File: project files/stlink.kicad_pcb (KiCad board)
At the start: 2 copper layers, 38.1 x 17.8 mm, 62 parts, among them J1 USB_C_Receptacle_USB2.0, J2 SWD, J3 SELF, J4 TARGET, Q1 MMBT9013, U1 STM32F103CBTx, U2 AMS1117-3.3, Y1 8MHz

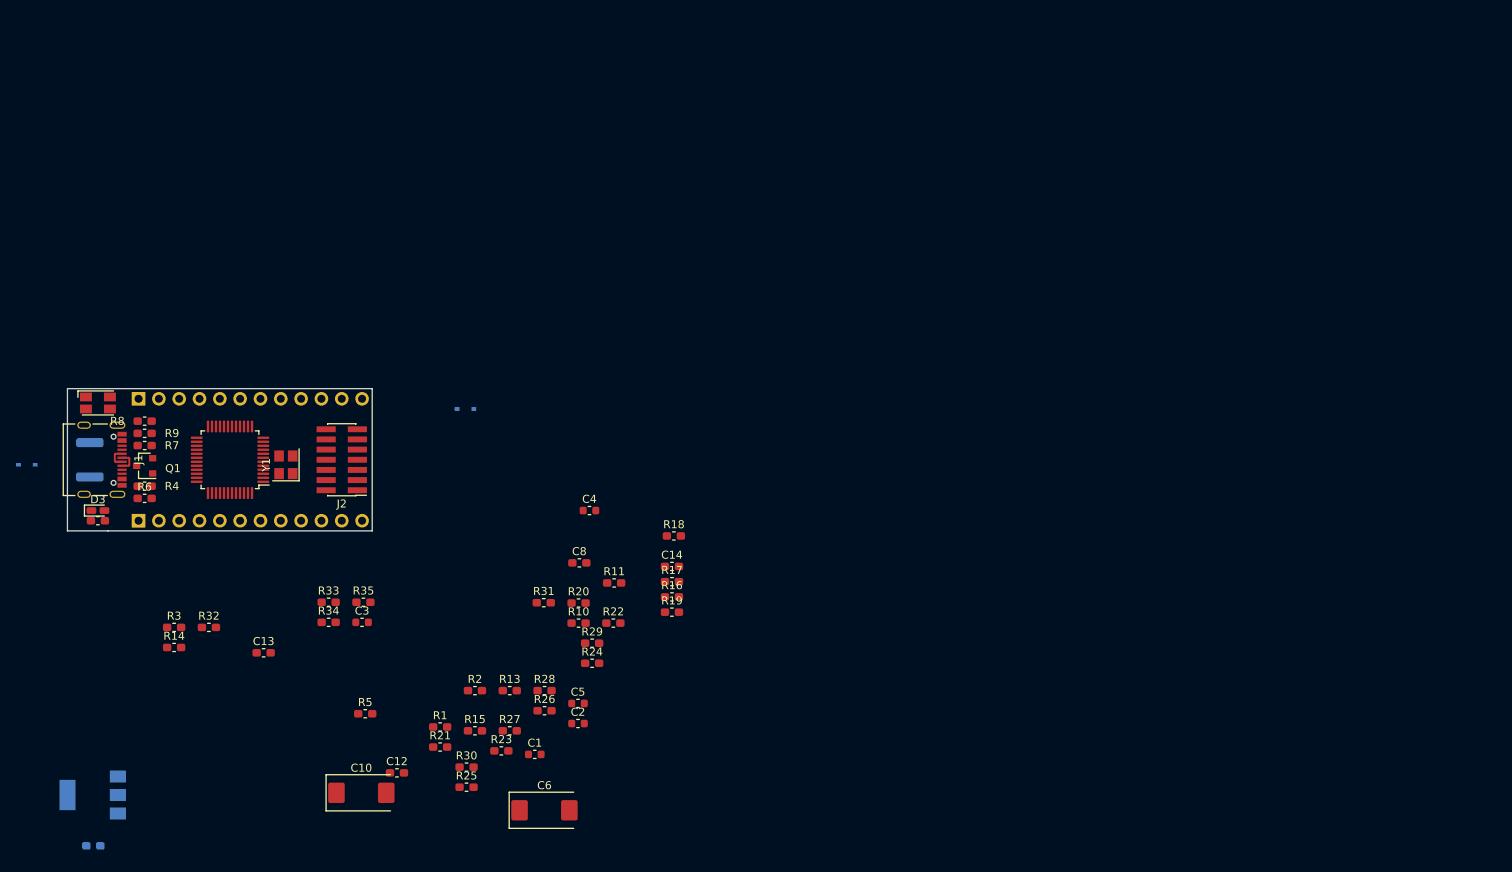
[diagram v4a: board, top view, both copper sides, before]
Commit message: Added possibility to power target from programmer
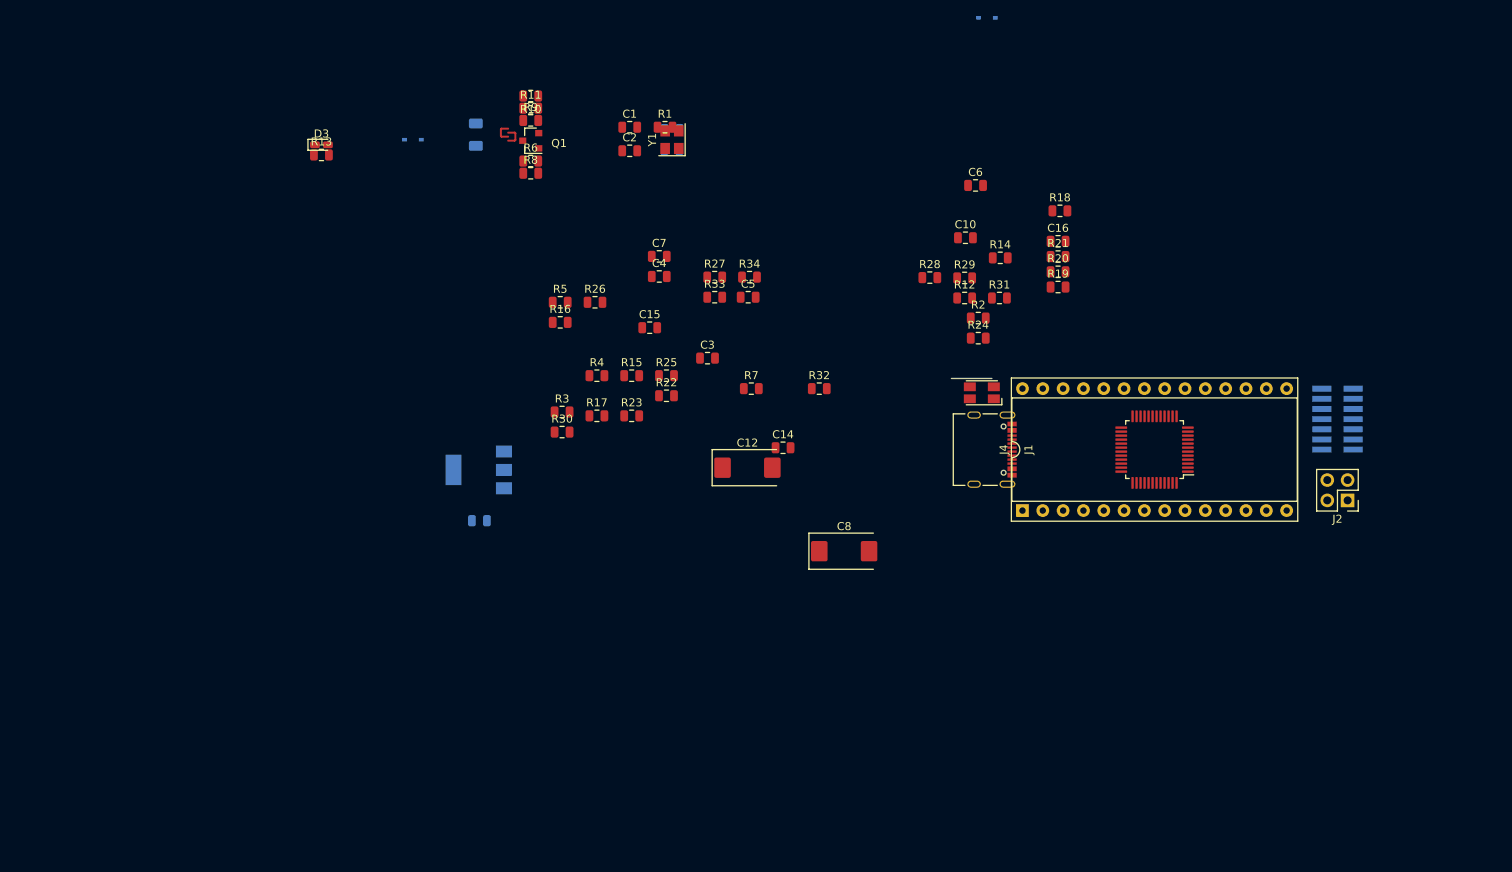
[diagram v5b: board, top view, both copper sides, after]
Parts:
- removed the J3 at (105.4, 125.7)
- removed the R23 at (150.8, 154.5)
- removed the R25 at (146.4, 159.0)
- removed the R30 at (146.4, 156.5)
- added C1: 100nF, Capacitor_SMD:C_0805_2012Metric, F.Cu at (166.8, 76.5)
- added C2: 1nF, Capacitor_SMD:C_0805_2012Metric, F.Cu at (166.8, 79.5)
- added J2: Power Target, Connector_PinHeader_2.54mm:PinHeader_2x02_P2.54mm_Vertical, F.Cu at (256.5, 123.2)
- added R1: 1M, Resistor_SMD:R_0805_2012Metric, F.Cu at (171.2, 76.5)
- added R32: 22R, Resistor_SMD:R_0805_2012Metric, F.Cu at (190.5, 109.2)
- C10: renamed from C8; footprint Capacitor_SMD:C_0603_1608Metric_Pad1.05x0.95mm_HandSolder -> Capacitor_SMD:C_0805_2012Metric
- C11: renamed from C9; footprint Capacitor_SMD:C_0603_1608Metric_Pad1.05x0.95mm_HandSolder -> Capacitor_SMD:C_0805_2012Metric
- C13: renamed from C11; footprint Capacitor_SMD:C_0603_1608Metric_Pad1.05x0.95mm_HandSolder -> Capacitor_SMD:C_0805_2012Metric
- C14: renamed from C12; footprint Capacitor_SMD:C_0603_1608Metric_Pad1.05x0.95mm_HandSolder -> Capacitor_SMD:C_0805_2012Metric
- C15: renamed from C13; footprint Capacitor_SMD:C_0603_1608Metric_Pad1.05x0.95mm_HandSolder -> Capacitor_SMD:C_0805_2012Metric
- C16: renamed from C14; footprint Capacitor_SMD:C_0603_1608Metric_Pad1.05x0.95mm_HandSolder -> Capacitor_SMD:C_0805_2012Metric
- C3: renamed from C1; footprint Capacitor_SMD:C_0603_1608Metric -> Capacitor_SMD:C_0805_2012Metric
- C4: renamed from C2; footprint Capacitor_SMD:C_0603_1608Metric -> Capacitor_SMD:C_0805_2012Metric
- C5: renamed from C3; footprint Capacitor_SMD:C_0603_1608Metric -> Capacitor_SMD:C_0805_2012Metric
- C6: renamed from C4; footprint Capacitor_SMD:C_0603_1608Metric -> Capacitor_SMD:C_0805_2012Metric
- C7: renamed from C5; footprint Capacitor_SMD:C_0603_1608Metric -> Capacitor_SMD:C_0805_2012Metric
- C9: renamed from C7; footprint Capacitor_SMD:C_0603_1608Metric_Pad1.05x0.95mm_HandSolder -> Capacitor_SMD:C_0805_2012Metric
- F1: footprint Fuse:Fuse_1812_4532Metric -> Resistor_SMD:R_1206_3216Metric
- J3: renamed from J2; moved to B.Cu
- J4: value TARGET -> Side Connectors; footprint Connector_PinHeader_2.54mm:PinHeader_1x12_P2.54mm_Vertical -> Package_DIP:DIP-28_W15.24mm_Socket; moved to F.Cu
- R10: renamed from R8; footprint Resistor_SMD:R_0603_1608Metric_Pad1.05x0.95mm_HandSolder -> Resistor_SMD:R_0805_2012Metric
- R11: renamed from R9; footprint Resistor_SMD:R_0603_1608Metric_Pad1.05x0.95mm_HandSolder -> Resistor_SMD:R_0805_2012Metric
- R12: renamed from R10; footprint Resistor_SMD:R_0603_1608Metric_Pad1.05x0.95mm_HandSolder -> Resistor_SMD:R_0805_2012Metric
- R13: renamed from R12; footprint Resistor_SMD:R_0603_1608Metric_Pad1.05x0.95mm_HandSolder -> Resistor_SMD:R_0805_2012Metric
- R14: renamed from R11; footprint Resistor_SMD:R_0603_1608Metric_Pad1.05x0.95mm_HandSolder -> Resistor_SMD:R_0805_2012Metric
- R15: renamed from R13; footprint Resistor_SMD:R_0603_1608Metric_Pad1.05x0.95mm_HandSolder -> Resistor_SMD:R_0805_2012Metric
- R16: renamed from R14; footprint Resistor_SMD:R_0603_1608Metric_Pad1.05x0.95mm_HandSolder -> Resistor_SMD:R_0805_2012Metric
- R17: renamed from R15; footprint Resistor_SMD:R_0603_1608Metric_Pad1.05x0.95mm_HandSolder -> Resistor_SMD:R_0805_2012Metric
- R18, R19, R24: footprint Resistor_SMD:R_0603_1608Metric_Pad1.05x0.95mm_HandSolder -> Resistor_SMD:R_0805_2012Metric
- R2: renamed from R29; footprint Resistor_SMD:R_0603_1608Metric_Pad1.05x0.95mm_HandSolder -> Resistor_SMD:R_0805_2012Metric
- R20: renamed from R16; footprint Resistor_SMD:R_0603_1608Metric_Pad1.05x0.95mm_HandSolder -> Resistor_SMD:R_0805_2012Metric
- R21: renamed from R17; footprint Resistor_SMD:R_0603_1608Metric_Pad1.05x0.95mm_HandSolder -> Resistor_SMD:R_0805_2012Metric
- R22: renamed from R26; footprint Resistor_SMD:R_0603_1608Metric_Pad1.05x0.95mm_HandSolder -> Resistor_SMD:R_0805_2012Metric
- R23: renamed from R27; footprint Resistor_SMD:R_0603_1608Metric_Pad1.05x0.95mm_HandSolder -> Resistor_SMD:R_0805_2012Metric
- R25: renamed from R28; footprint Resistor_SMD:R_0603_1608Metric_Pad1.05x0.95mm_HandSolder -> Resistor_SMD:R_0805_2012Metric
- R26: renamed from R32; footprint Resistor_SMD:R_0603_1608Metric_Pad1.05x0.95mm_HandSolder -> Resistor_SMD:R_0805_2012Metric
- R27: renamed from R33; footprint Resistor_SMD:R_0603_1608Metric_Pad1.05x0.95mm_HandSolder -> Resistor_SMD:R_0805_2012Metric
- R28: renamed from R31; footprint Resistor_SMD:R_0603_1608Metric_Pad1.05x0.95mm_HandSolder -> Resistor_SMD:R_0805_2012Metric
- R29: renamed from R20; footprint Resistor_SMD:R_0603_1608Metric_Pad1.05x0.95mm_HandSolder -> Resistor_SMD:R_0805_2012Metric
- R3: renamed from R1; footprint Resistor_SMD:R_0603_1608Metric_Pad1.05x0.95mm_HandSolder -> Resistor_SMD:R_0805_2012Metric
- R30: renamed from R21; footprint Resistor_SMD:R_0603_1608Metric_Pad1.05x0.95mm_HandSolder -> Resistor_SMD:R_0805_2012Metric
- R31: renamed from R22; footprint Resistor_SMD:R_0603_1608Metric_Pad1.05x0.95mm_HandSolder -> Resistor_SMD:R_0805_2012Metric
- R33: renamed from R34; footprint Resistor_SMD:R_0603_1608Metric_Pad1.05x0.95mm_HandSolder -> Resistor_SMD:R_0805_2012Metric
- R34: renamed from R35; footprint Resistor_SMD:R_0603_1608Metric_Pad1.05x0.95mm_HandSolder -> Resistor_SMD:R_0805_2012Metric
- R4: renamed from R2; footprint Resistor_SMD:R_0603_1608Metric_Pad1.05x0.95mm_HandSolder -> Resistor_SMD:R_0805_2012Metric
- R5: renamed from R3; footprint Resistor_SMD:R_0603_1608Metric_Pad1.05x0.95mm_HandSolder -> Resistor_SMD:R_0805_2012Metric
- R6: renamed from R4; footprint Resistor_SMD:R_0603_1608Metric_Pad1.05x0.95mm_HandSolder -> Resistor_SMD:R_0805_2012Metric
- R7: renamed from R5; footprint Resistor_SMD:R_0603_1608Metric_Pad1.05x0.95mm_HandSolder -> Resistor_SMD:R_0805_2012Metric
- R8: renamed from R6; footprint Resistor_SMD:R_0603_1608Metric_Pad1.05x0.95mm_HandSolder -> Resistor_SMD:R_0805_2012Metric
- R9: renamed from R7; footprint Resistor_SMD:R_0603_1608Metric_Pad1.05x0.95mm_HandSolder -> Resistor_SMD:R_0805_2012Metric
- moved J3 124.6 mm to (255.3, 113.0), turned to 0 degrees
- moved U1 115.6 mm to (232.4, 116.8)
- moved J4 111.4 mm to (215.9, 124.5), turned to 90 degrees
- moved J1 111.3 mm to (212.1, 116.8)
- moved D2 110.5 mm to (210.8, 109.7), turned to 180 degrees
- moved D4 81.5 mm to (211.5, 62.9)
- moved C12 63.1 mm to (181.5, 119.1)
- moved C10 63.1 mm to (208.8, 90.4)
- moved C13 63.1 mm to (148.0, 125.7)
- moved C5 63.1 mm to (181.6, 97.8)
- moved F1 63.1 mm to (147.6, 77.5)
- moved R18 63.1 mm to (220.6, 87.0)
- moved R31 63.1 mm to (213.0, 97.9)
- moved R33 63.1 mm to (177.4, 97.8)
- moved C11 63.1 mm to (172.1, 76.8)
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- renumbered C10 to C12, C6 to C8
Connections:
- net /T_JTCK renamed /T_SWDCLK
- net /T_JTMS renamed /T_SWDIO
- C10 pad 2: GNDREF -> GND_detect(h)
- C11 pad 2: GNDREF -> GND_detect(h)
- C12 pad 2: GNDREF -> GND_detect(h)
- C13 pad 2: GNDREF -> GND_detect(h)
- C14 pad 1: BOOT_0h -> BOOT_0(h)
- C14 pad 2: GNDREF -> GND_detect(h)
- C15 pad 1: Self_NRSTh -> Self_NRST(h)
- C15 pad 2: GNDREF -> GND_detect(h)
- C16 pad 1: /AIN -> GND_detect(h)
- C16 pad 2: GNDREF -> /AIN
- C3 pad 2: GNDREF -> GND_detect(h)
- C4 pad 2: GNDREF -> GND_detect(h)
- C5 pad 2: GNDREF -> GND_detect(h)
- C6 pad 2: GNDREF -> GND_detect(h)
- C7 pad 2: GNDREF -> GND_detect(h)
- C8 pad 2: GNDREF -> GND_detect(h)
- C9 pad 2: GNDREF -> GND_detect(h)
- D2 pad 1: Net-(D2-Pad1) -> GND_detect(h)
- D2 pad 2: GNDREF -> Net-(D2-Pad2)
- D3 pad 1: GNDREF -> GND_detect(h)
- J1 pad A1: GNDREF -> GND_detect(h)
- J1 pad A12: GNDREF -> GND_detect(h)
- J1 pad A8: Net-(J1-PadA8) -> (no net)
- J1 pad B1: GNDREF -> GND_detect(h)
- J1 pad B12: GNDREF -> GND_detect(h)
- J1 pad B8: Net-(J1-PadB8) -> (no net)
- J1 pad S1: GNDREF -> Net-(C1-Pad1)
- J3 pad 1: Net-(J2-Pad1) -> (no net)
- J3 pad 12: T_NRST_SWDh -> T_NRST_SWD(h)
- J3 pad 13: T_VCP_RXh -> T_VCP_RX(h)
- J3 pad 14: T_VCP_TXh -> T_VCP_TX(h)
- J3 pad 2: Net-(J2-Pad2) -> (no net)
- J3 pad 4: T_JTMS-T_SWDIO(h) -> T_SWDIO(h)
- J3 pad 5: GNDREF -> GND_detect(h)
- J3 pad 6: T_JTLK(h) -> T_SWDCLK(h)
- J3 pad 7: GNDREF -> GND_detect(h)
- J3 pad 8: T_JTDO-T_SWO(h) -> T_SWO(h)
- J3 pad 9: T_JTLK(h) -> (no net)
- J4 pad 1: T_Vref -> +5V
- J4 pad 10: T_SWDIOh -> Self_SWDCLK(h)
- J4 pad 11: T_NRST_SWDh -> GND_detect(h)
- J4 pad 12: T_SWOh -> Self_SWDIO(h)
- J4 pad 2: T_SWIMh -> +3V3
- J4 pad 3: GNDREF -> BOOT_0(h)
- J4 pad 4: T_NRST_SWIMh -> +3V3
- J4 pad 5: T_VCP_RXh -> Self_TX(h)
- J4 pad 6: T_VCP_TXh -> Self_RX(h)
- J4 pad 7: T_Vref -> GND_detect(h)
- J4 pad 8: T_SWDCLKh -> (no net)
- J4 pad 9: GNDREF -> +3V3
- R12 pad 1: GNDREF -> GND_detect(h)
- R13 pad 1: Net-(D2-Pad1) -> /STLINK_LED
- R13 pad 2: /STLINK_LED -> Net-(D2-Pad2)
- R15 pad 1: BOOT_0h -> BOOT_0(h)
- R15 pad 2: GNDREF -> GND_detect(h)
- R17 pad 1: Self_NRSTh -> Self_NRST(h)
- R18 pad 2: GNDREF -> GND_detect(h)
- R2 pad 1: /PC13 -> GND_detect(h)
- R2 pad 2: GNDREF -> Net-(R2-Pad2)
- R21 pad 2: GNDREF -> GND_detect(h)
- R26 pad 2: T_SWIMh -> T_SWIM(h)
- R27 pad 2: T_NRST_SWIMh -> T_NRST_SWIM(h)
- R28 pad 1: T_JTMS-T_SWDIO(h) -> T_SWDIO(h)
- R29 pad 1: T_NRST_SWDh -> T_NRST_SWD(h)
- R3 pad 2: GNDREF -> GND_detect(h)
- R30 pad 1: T_JTLK(h) -> T_SWDCLK(h)
- R31 pad 1: T_JTDO-T_SWO(h) -> T_SWO(h)
- R33 pad 1: T_VCP_TXh -> T_VCP_TX(h)
- R34 pad 1: T_VCP_RXh -> T_VCP_RX(h)
- R4 pad 2: GNDREF -> GND_detect(h)
- R5 pad 2: Self_TXh -> Self_TX(h)
- R9 pad 2: Self_RXh -> Self_RX(h)
- U1 pad 11: Net-(U1-Pad11) -> (no net)
- U1 pad 14: Net-(U1-Pad14) -> (no net)
- U1 pad 16: /T_JTDO -> (no net)
- U1 pad 19: /T_JRST -> (no net)
- U1 pad 2: /PC13 -> Net-(R2-Pad2)
- U1 pad 20: GNDREF -> GND_detect(h)
- U1 pad 23: GNDREF -> GND_detect(h)
- U1 pad 28: Net-(U1-Pad28) -> (no net)
- U1 pad 29: Net-(U1-Pad29) -> (no net)
- U1 pad 3: /PC14 -> (no net)
- U1 pad 30: Self_TXh -> Self_TX(h)
- U1 pad 31: Self_RXh -> Self_RX(h)
- U1 pad 34: Self_SWDIOh -> Self_SWDIO(h)
- U1 pad 35: GNDREF -> GND_detect(h)
- U1 pad 37: Self_SWDCLKh -> Self_SWDCLK(h)
- U1 pad 39: Self_SWOh -> Self_SWO(h)
- U1 pad 4: Net-(U1-Pad4) -> (no net)
- U1 pad 40: Net-(U1-Pad40) -> (no net)
- U1 pad 44: BOOT_0h -> BOOT_0(h)
- U1 pad 47: GNDREF -> GND_detect(h)
- U1 pad 7: Self_NRSTh -> Self_NRST(h)
- U1 pad 8: GNDREF -> GND_detect(h)
- U2 pad 1: GNDREF -> GND_detect(h)
- Y1 pad 2: Net-(Y1-Pad2) -> GND_detect(h)
- Y1 pad 4: Net-(Y1-Pad4) -> GND_detect(h)
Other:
- board outline removed

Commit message: minor tracing
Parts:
- removed the J4 at (215.9, 124.5)
- added J3: Self, Connector_PinHeader_2.54mm:PinHeader_1x14_P2.54mm_Vertical, B.Cu at (215.9, 124.5)
- added J5: Target, Connector_PinHeader_2.54mm:PinHeader_1x14_P2.54mm_Vertical, B.Cu at (215.9, 109.2)
- added U2: STM32F103CBUx, Package_DFN_QFN:QFN-48-1EP_7x7mm_P0.5mm_EP5.6x5.6mm, F.Cu at (232.4, 116.8)
- J1: value USB_C_Receptacle_USB2.0 -> USB Type C
- J4: renamed from J3; value SWD -> STDC-14; moved to F.Cu
- moved C9 78.0 mm to (239.3, 116.5)
- moved Y1 77.9 mm to (239.3, 117.6)
- moved C8 77.9 mm to (239.3, 118.7)
- moved Q1 73.6 mm to (216.7, 117.6)
- moved R8 73.6 mm to (216.7, 115.1)
- moved R10 73.6 mm to (216.7, 113.5)
- moved R5 73.6 mm to (216.7, 120.1)
- moved R7 73.6 mm to (216.7, 121.7)
- moved R9 73.6 mm to (216.7, 112.0)
- moved J2 46.4 mm to (210.2, 121.9), turned to 0 degrees
- moved J4 9.63 mm to (246.4, 116.8), turned to 180 degrees
- moved R1 5.89 mm to (168.9, 71.1)
- moved J1 0.76 mm to (211.3, 116.8)
- moved D2 0.64 mm to (211.5, 109.7)
- renumbered C8 to C10, C14 to C11, C15 to C12, C10 to C13, C12 to C14, C13 to C15, C5 to C4, C4 to C5, C9 to C8, C11 to C9, D4 to D3, D3 to D4, R11 to R10, R12 to R11, R13 to R12, R14 to R13, R15 to R14, R2 to R15, R17 to R16, R18 to R17, R16 to R18, R3 to R2, R4 to R3, R5 to R4, R6 to R5, R7 to R6, R8 to R7, R9 to R8, R10 to R9, U2 to U3
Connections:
- net Net-(R2-Pad2) renamed /Board_ID
- C4 pad 1: +3V3 -> Net-(C4-Pad1)
- C6 pad 1: +3V3 -> Net-(C4-Pad1)
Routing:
- net /STLINK_OSC_IN: track 0.00 -> 4.56 mm
- net /D-: track 2.72 -> 0.00 mm
- net /D+: track 2.71 -> 0.00 mm
- net /STLINK_OST_OUT: track 0.00 -> 2.09 mm
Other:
- board outline added: 52.1 x 17.8 mm

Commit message: new references
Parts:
- C1, C16, C2: footprint Capacitor_SMD:C_0805_2012Metric -> Capacitor_SMD:C_0603_1608Metric; moved to B.Cu
- C11, C12, C13, C15, C3, C4, C5, C6, C7, C8, C9: footprint Capacitor_SMD:C_0805_2012Metric -> Capacitor_SMD:C_0603_1608Metric
- Q1: moved to B.Cu
- R1, R15, R17, R19, R20, R21, R8: footprint Resistor_SMD:R_0805_2012Metric -> Resistor_SMD:R_0603_1608Metric; moved to B.Cu
- R10, R11, R12, R13, R14, R16, R18, R2, R22, R23, R24, R25, R26, R27, R28, R29, R3, R30, R31, R32, R33, R34, R4, R5, R6, R7, R9: footprint Resistor_SMD:R_0805_2012Metric -> Resistor_SMD:R_0603_1608Metric
- moved J2 61.2 mm to (271.1, 127.0)
- moved R1 60.7 mm to (210.2, 115.6), turned to 180 degrees
- moved C1 59.6 mm to (210.2, 117.5)
- moved C2 58.9 mm to (210.2, 119.4)
- moved R15 34.1 mm to (238.1, 120.2), turned to 90 degrees
- moved D3 30.4 mm to (224.8, 90.2)
- moved R8 9.45 mm to (226.1, 116.1), turned to 270 degrees
- moved R5 3.94 mm to (216.7, 116.2)
- moved R7 3.56 mm to (216.7, 118.1)
- moved R17 1.92 mm to (220.3, 88.9), turned to 180 degrees
- turned R19 to 180 degrees
- turned R21 to 180 degrees
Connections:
- C4 pad 1: Net-(C4-Pad1) -> +3V3
- C6 pad 1: Net-(C4-Pad1) -> +3V3
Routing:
- net /STLINK_OSC_IN: track 4.56 -> 0.00 mm
- net /STLINK_OST_OUT: track 2.09 -> 0.00 mm
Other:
- board size 52.1 x 17.8 mm -> 43.2 x 17.8 mm

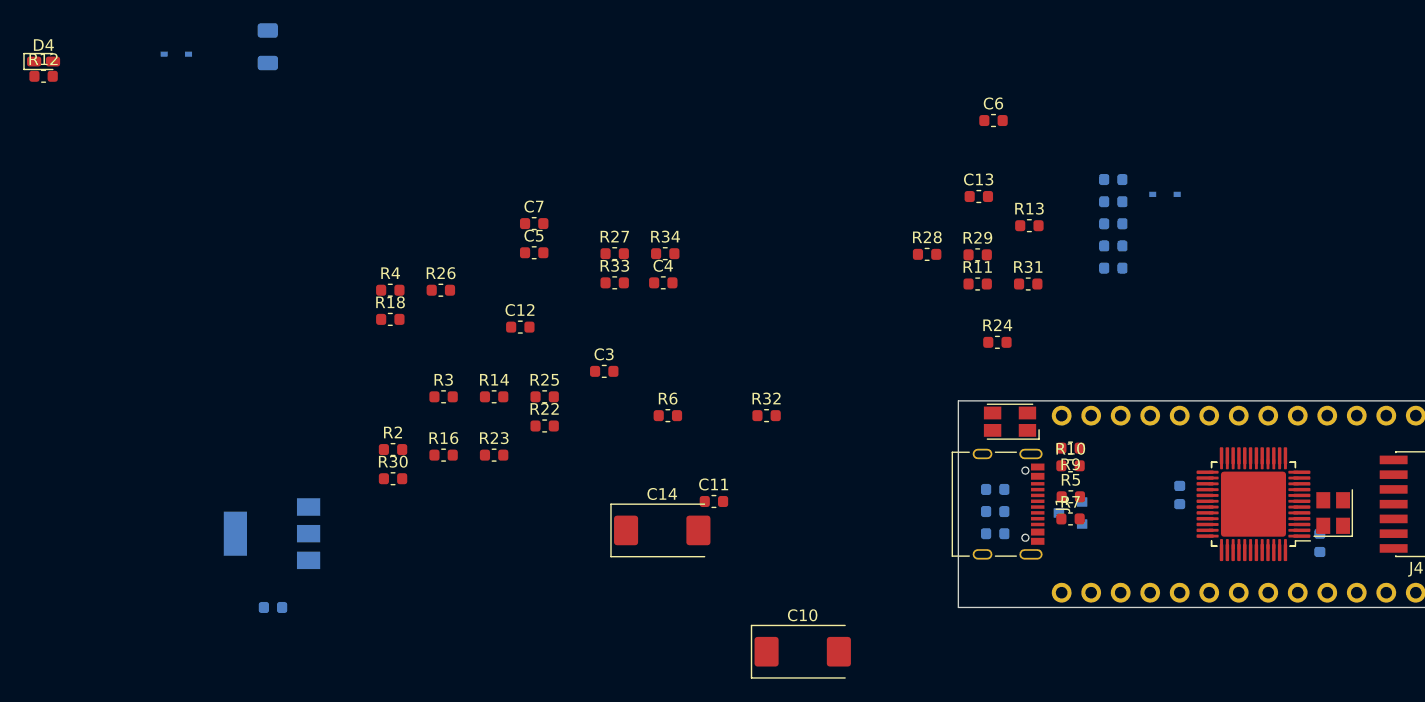
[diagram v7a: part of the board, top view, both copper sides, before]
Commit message: added reference for BMP
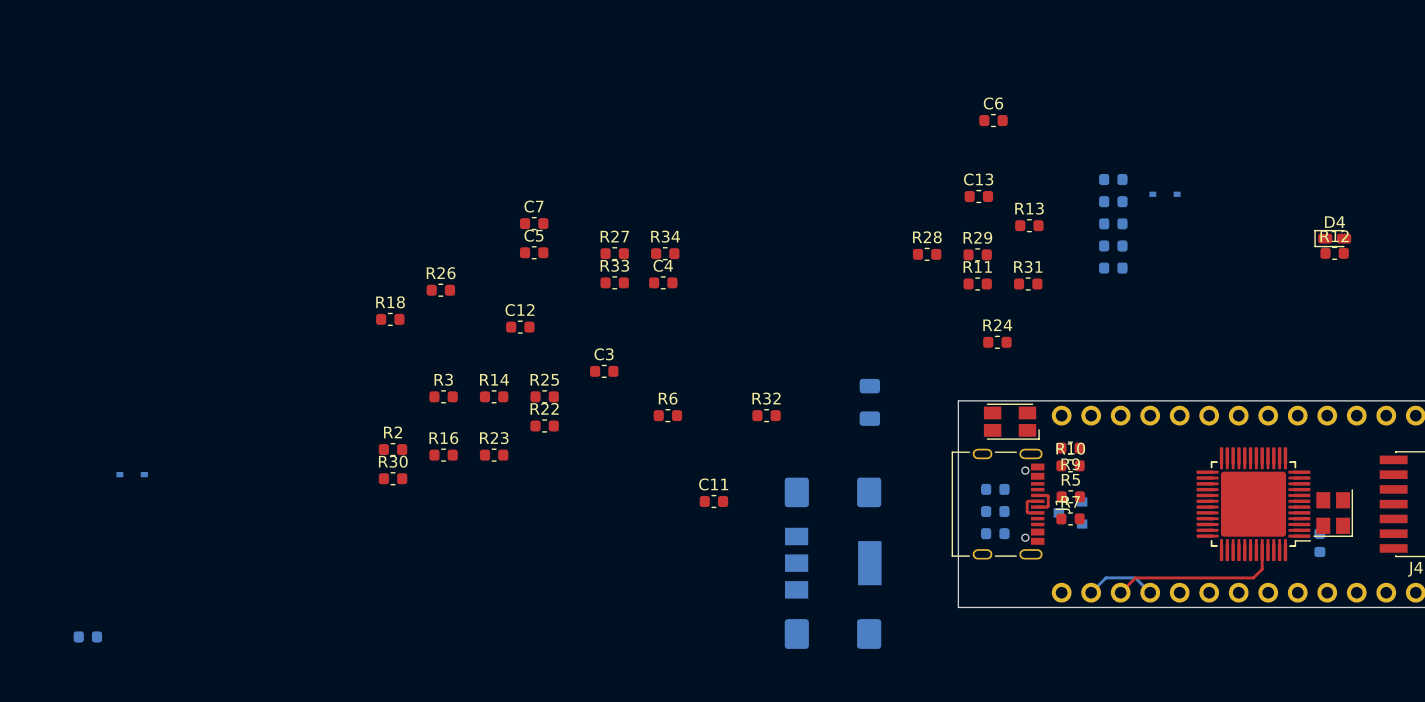
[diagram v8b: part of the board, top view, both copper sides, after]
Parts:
- removed R4, R8: 10R, Resistor_SMD:R_0603_1608Metric
- C10, C14: moved to B.Cu
- moved D4 112.2 mm to (239.4, 94.0)
- moved R12 112.2 mm to (239.4, 95.2)
- moved F1 60.2 mm to (199.4, 108.1)
- moved U3 48.4 mm to (196.2, 121.9), turned to 0 degrees
- moved D1 36.4 mm to (135.9, 114.3)
- moved C14 17.2 mm to (196.2, 128.0), turned to 180 degrees
- moved C15 16.1 mm to (132.1, 128.3)
- moved C10 14.0 mm to (196.2, 115.8), turned to 180 degrees
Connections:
- C11 pad 1: BOOT_0(h) -> GND_detect(h)
- C11 pad 2: GND_detect(h) -> BOOT_0(h)
- C12 pad 1: Self_NRST(h) -> GND_detect(h)
- C12 pad 2: GND_detect(h) -> Self_NRST(h)
- R12 pad 1: /STLINK_LED -> Net-(D2-Pad3)
- R12 pad 2: Net-(D2-Pad2) -> Self_TX(h)
- R13 pad 1: Net-(D2-Pad3) -> Net-(D2-Pad2)
- R13 pad 2: /STLINK_LED -> Self_TX(h)
- R31 pad 2: /T_SWO -> Self_RX(h)
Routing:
- net BOOT_0(h): track 0.00 -> 14.5 mm
- net +3V3: track 0.00 -> 6.13 mm
- net /D+: track 0.00 -> 2.72 mm
- net /D-: track 0.00 -> 2.71 mm
